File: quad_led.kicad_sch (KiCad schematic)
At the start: 9 parts

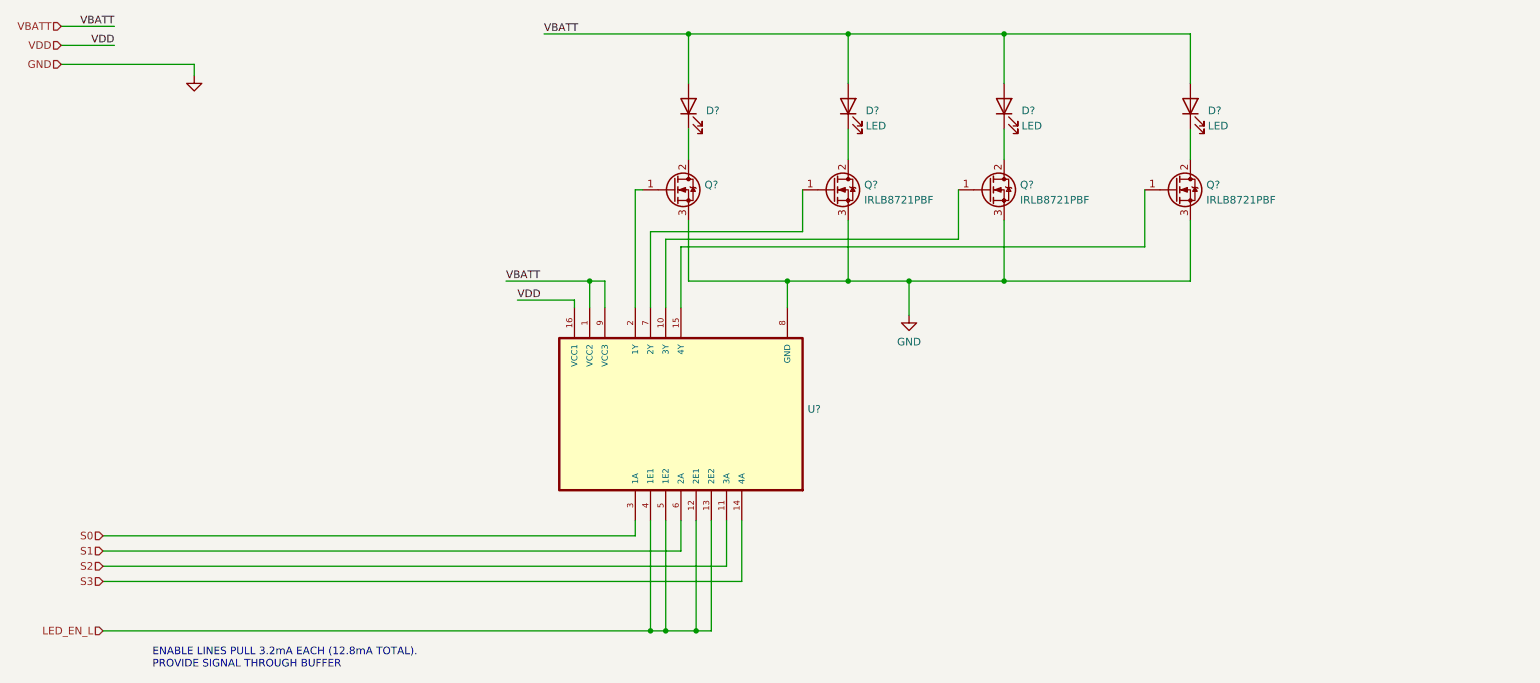
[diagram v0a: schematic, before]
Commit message: Add schematic for button inputs and I2C signal busses.
* Define 9x button inputs
* Define I2C parallel bus expanders used for FET output signals
  and button inputs
* Add (empty) schematic for 5V switching regulator.
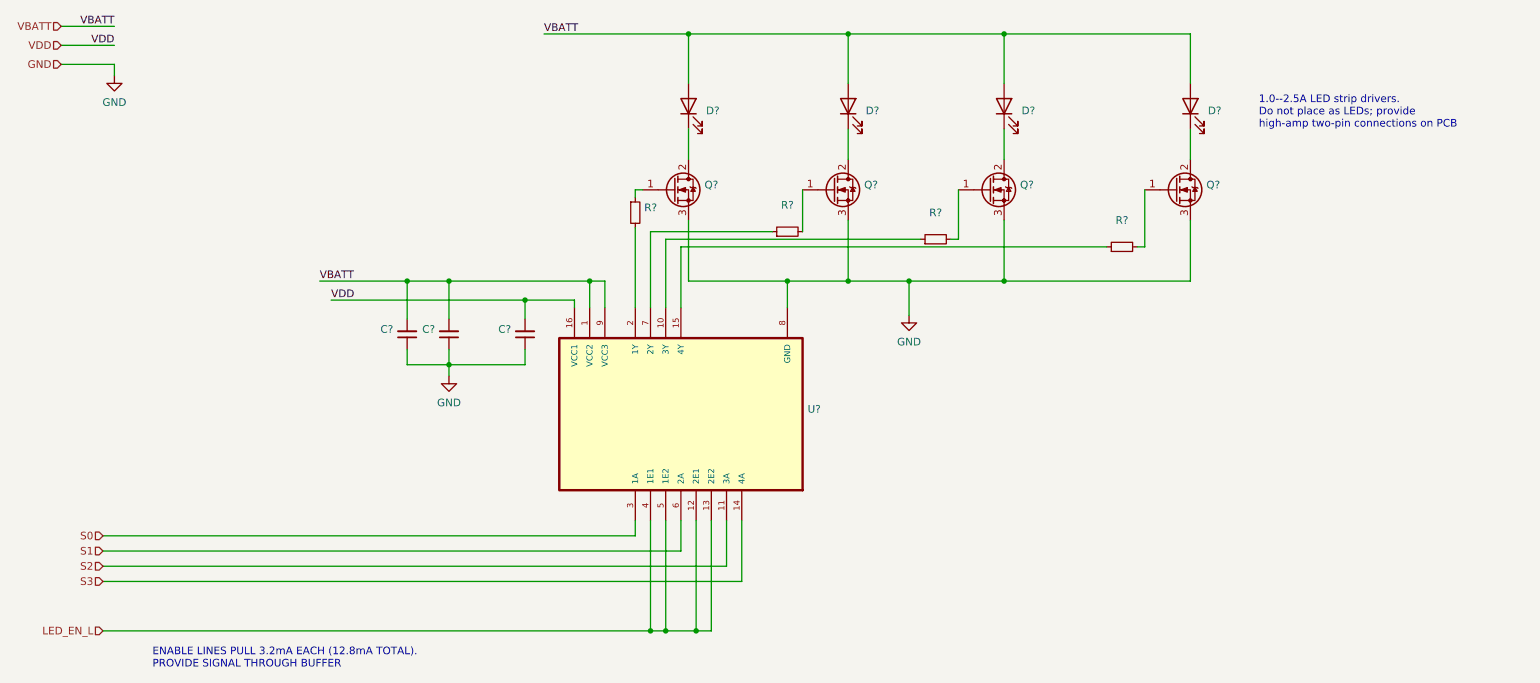
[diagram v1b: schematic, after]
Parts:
- added C? (x3): (no value), symbol Device:C_Small
- added R? (x4): (no value), symbol Device:R_Small
- D? (x3): value LED -> (none)
- Q? (x3): value IRLB8721PBF -> (none); footprint Package_TO_SOT_THT:TO-220-3_Vertical -> (none)
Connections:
- net GND: now also C?.1, C?.1, C?.1
- net VBATT: now also C?.2, C?.2
- net VDD: now also C?.2
- net at Q?.1 (G): now also R?.1; no longer U?.2 (1Y)
- net at U?.10 (3Y): now also R?.1; no longer Q?.1 (G)
- net at U?.15 (4Y): now also R?.1; no longer Q?.1 (G)
- net at U?.7 (2Y): now also R?.1; no longer Q?.1 (G)
- new net: Q?.1 (G), R?.2 (x3)
- new net: R?.2, U?.2 (1Y)
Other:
- note added: "1.0--2.5A LED strip drivers. Do not place as LEDs; provide high-amp two-pin connections on PCB"

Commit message: Sketch out ISL8117-driven 12V regulator.
Another candidate entry for on-board 12V regulation is to
build our own based on the reference schematic from the ISL8117
DC buck regulator controller datasheet.

Implemented (most of) this reference schematic here.
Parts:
- added R? (x5): (no value), symbol Device:R_Small
- C?: value (none) -> 1u
- C? (x2): value (none) -> 100n
- D? (x4): value (none) -> LED
- Q? (x4): value (none) -> IRLB8721PBF; footprint (none) -> Package_TO_SOT_THT:TO-220-3_Vertical
- U?: value (none) -> SN75374N; footprint (none) -> Aaron_TI_Parts:TI_N_R-PDIP-T16
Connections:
- net LED_EN_L: now also R?.1; no longer U?.12 (2E1), U?.13 (2E2), U?.4 (1E1), U?.5 (1E2)
- net S0: now also R?.1; no longer U?.3 (1A)
- net S1: now also R?.1; no longer U?.6 (2A)
- net S2: now also R?.1; no longer U?.11 (3A)
- net S3: now also R?.1; no longer U?.14 (4A)
- new net: R?.2, U?.11 (3A)
- new net: R?.2, U?.12 (2E1), U?.13 (2E2), U?.4 (1E1), U?.5 (1E2)
- new net: R?.2, U?.14 (4A)
- new net: R?.2, U?.3 (1A)
- new net: R?.2, U?.6 (2A)
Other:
- note added: "ENABLE LINES PULL 2mA EACH (3.2mA MAX) - 8mA TOTAL. PROVIDE SIGNAL THROUGH BUFFER"
- note added: "Signal lines 1mA max"
- note removed: "ENABLE LINES PULL 3.2mA EACH (12.8mA TOTAL). PROVIDE SIGNAL THROUGH BUFFER"
